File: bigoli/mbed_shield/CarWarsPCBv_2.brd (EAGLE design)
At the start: 68.6 x 55.9 mm, 22 parts, among them J1 MAGJACK, Q1 220mA/50V/3.5Ω, Q2 220mA/50V/3.5Ω

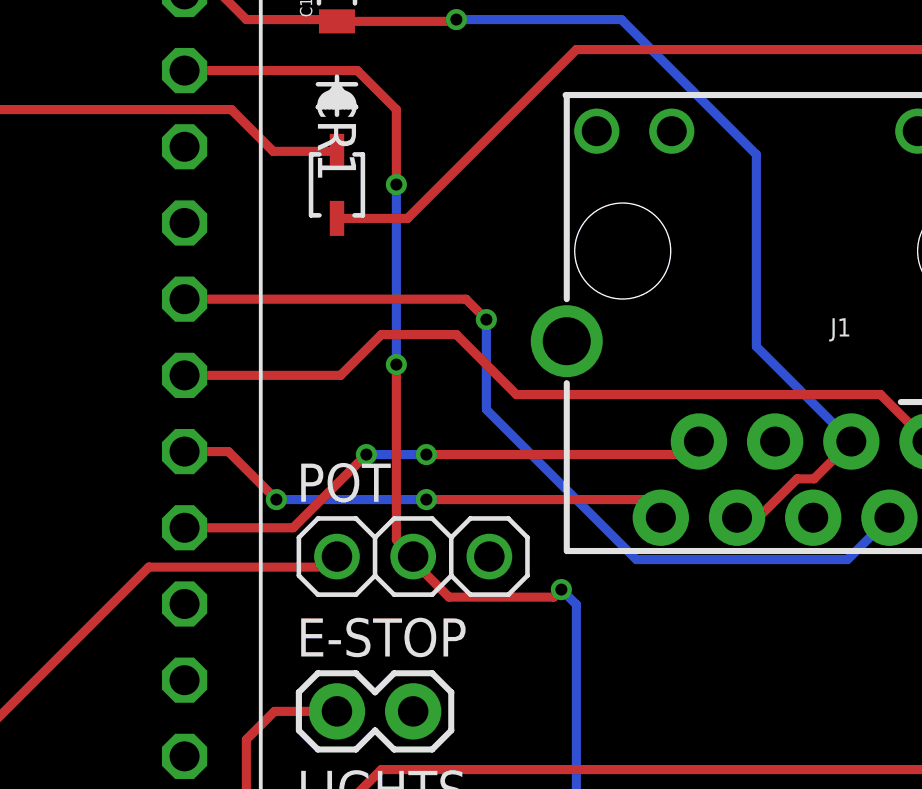
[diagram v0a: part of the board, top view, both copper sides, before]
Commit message: Fixed Routing so Pot runs at 3v3.  Added Resistor and Capacitor Values.
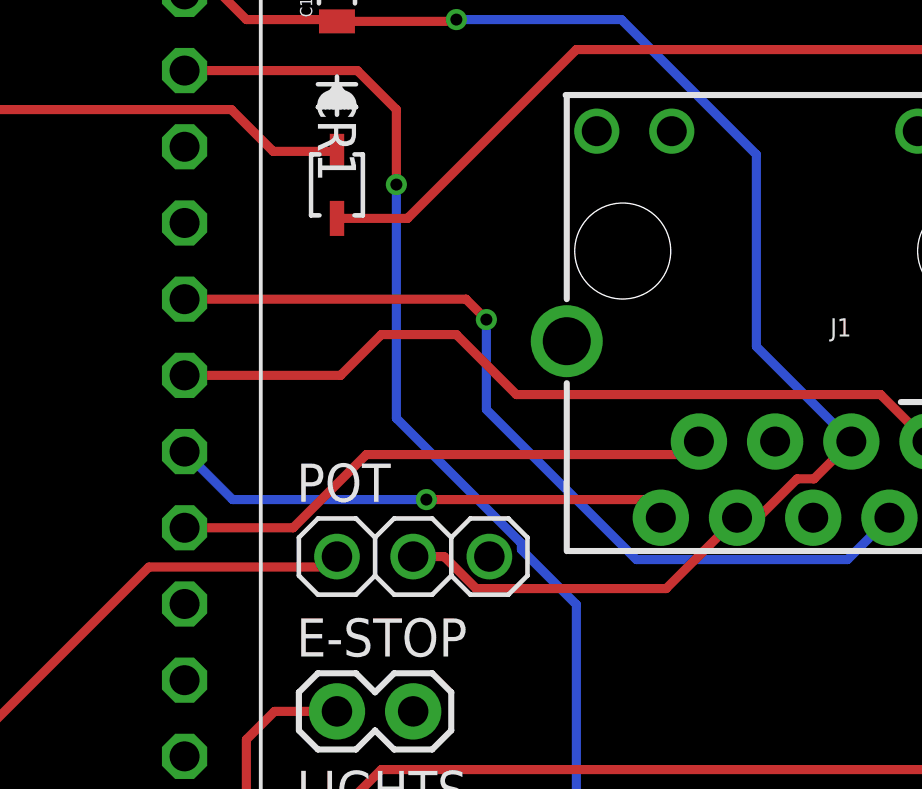
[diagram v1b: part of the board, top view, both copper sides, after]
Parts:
- C2: value (none) -> 1000PF
- R5, R6: value 62 -> 1K
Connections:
- net +3V3: now also POT.2
- net +5V: no longer POT.2
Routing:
- net +3V3: track 37.1 -> 49.3 mm
- net +5V: track 77.5 -> 75.0 mm, vias 4 -> 2
- net ETH_TD+: track 18.3 -> 18.9 mm, vias 2 -> 0
- net ETH_TD-: vias 2 -> 1
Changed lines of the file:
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@@
 <?xml version="1.0" encoding="utf-8"?>
 <!DOCTYPE eagle SYSTEM "eagle.dtd">
-<eagle version="8.2.1">
+<eagle version="8.3.2">
 <drawing>
 <settings>
 <setting alwaysvectorfont="no"/>
+<setting keepoldvectorfont="yes"/>
 <setting verticaltext="up"/>
 </settings>
@@
 <layers>
 <layer number="1" name="Top" color="4" fill="1" visible="yes" active="yes"/>
-<layer number="2" name="Route2" color="1" fill="3" visible="no" active="yes"/>
+<layer number="2" name="Route2" color="1" fill="3" visible="yes" active="yes"/>
 <layer number="3" name="Route3" color="4" fill="3" visible="no" active="yes"/>
 <layer number="4" name="Route4" color="1" fill="4" visible="no" active="yes"/>
@@
 <element name="R3" library="rcl" library_urn="urn:adsk.eagle:library:334" package="R0603" value="10K" x="49.76" y="21.82" rot="R270"/>
 <element name="R4" library="rcl" library_urn="urn:adsk.eagle:library:334" package="R0603" value="10K" x="49.76" y="10.35" rot="R90"/>
-<element name="R5" library="rcl" library_urn="urn:adsk.eagle:library:334" package="R0603" value="62" x="53.57" y="10.35" rot="R270"/>
-<element name="R6" library="rcl" library_urn="urn:adsk.eagle:library:334" package="R0603" value="62" x="53.57" y="21.82" rot="R90"/>
+<element name="R5" library="rcl" library_urn="urn:adsk.eagle:library:334" package="R0603" value="1K" x="53.57" y="10.35" rot="R270"/>
+<element name="R6" library="rcl" library_urn="urn:adsk.eagle:library:334" package="R0603" value="1K" x="53.57" y="21.82" rot="R90"/>
 <element name="STEER" library="Roboracing" package="1X03" value="" x="35.56" y="9.2"/>
-<element name="C2" library="rcl" library_urn="urn:adsk.eagle:library:334" package="C0805" value="" x="60.96" y="38.1"/>
+<element name="C2" library="rcl" library_urn="urn:adsk.eagle:library:334" package="C0805" value="1000PF" x="60.96" y="38.1"/>
 </elements>
 <signals>
@@
 <wire x1="43.21" y1="36.5" x2="36" y2="36.5" width="0.3048" layer="1"/>
 <via x="36" y="36.5" extent="1-16" drill="0.4"/>
-<wire x1="36" y1="36.5" x2="31" y2="36.5" width="0.3048" layer="16"/>
-<via x="31" y="36.5" extent="1-16" drill="0.4"/>
-<wire x1="31" y1="36.5" x2="29.4" y2="38.1" width="0.3048" layer="1"/>
-<wire x1="29.4" y1="38.1" x2="27.94" y2="38.1" width="0.3048" layer="1"/>
+<wire x1="36" y1="36.5" x2="29.54" y2="36.5" width="0.3048" layer="16"/>
+<wire x1="29.54" y1="36.5" x2="27.94" y2="38.1" width="0.3048" layer="16"/>
 </signal>
 <signal name="ETH_TD+">
 <contactref element="MBED" pad="33"/>
 <contactref element="J1" pad="7"/>
-<via x="36" y="38" extent="1-16" drill="0.4"/>
-<wire x1="36" y1="38" x2="34" y2="38" width="0.3048" layer="16"/>
-<via x="34" y="38" extent="1-16" drill="0.4"/>
-<wire x1="36" y1="38" x2="44.65" y2="38" width="0.3048" layer="1"/>
-<wire x1="44.65" y1="38" x2="45.085" y2="38.435" width="0.3048" layer="1"/>
+<wire x1="45.075" y1="38.425" x2="45.085" y2="38.435" width="0.3048" layer="1"/>
+<wire x1="45.075" y1="38.425" x2="44.65" y2="38" width="0.3048" layer="1"/>
 <wire x1="27.94" y1="35.56" x2="31.56" y2="35.56" width="0.3048" layer="1"/>
 <wire x1="31.56" y1="35.56" x2="34" y2="38" width="0.3048" layer="1"/>
+<wire x1="34" y1="38" x2="44.65" y2="38" width="0.3048" layer="1"/>
+<wire x1="44.65" y1="38" x2="45.075" y2="38.425" width="0.3048" layer="1"/>
 </signal>
 <signal name="GND">
@@
 <wire x1="46.355" y1="35.895" x2="47.063025" y2="35.895" width="0.3048" layer="1"/>
 <wire x1="47.063025" y1="35.895" x2="48.358425" y2="37.1904" width="0.3048" layer="1"/>
+<contactref element="POT" pad="2"/>
+<wire x1="35.56" y1="34.6" x2="36.5913125" y2="34.6" width="0.3048" layer="1"/>
+<wire x1="36.5913125" y1="34.6" x2="37.6581125" y2="33.5332" width="0.3048" layer="1"/>
+<wire x1="37.6581125" y1="33.5332" x2="43.9932" y2="33.5332" width="0.3048" layer="1"/>
+<wire x1="43.9932" y1="33.5332" x2="46.355" y2="35.895" width="0.3048" layer="1"/>
 </signal>
 <signal name="DRIVE_PWM_3V3">
@@
 <contactref element="MBED" pad="39"/>
 <contactref element="ENCODER" pad="4"/>
-<contactref element="POT" pad="2"/>
 <contactref element="R5" pad="2"/>
 <contactref element="R6" pad="2"/>
@@
 <wire x1="35" y1="49.5" x2="35" y2="47" width="0.3048" layer="1"/>
 <via x="35" y="47" extent="1-16" drill="0.4"/>
-<wire x1="35" y1="47" x2="35" y2="41" width="0.3048" layer="16"/>
-<via x="35" y="41" extent="1-16" drill="0.4"/>
-<wire x1="35" y1="35.16" x2="35" y2="41" width="0.3048" layer="1"/>
-<wire x1="35" y1="35.16" x2="35.56" y2="34.6" width="0.3048" layer="1"/>
-<via x="40.5" y="33.5" extent="1-16" drill="0.4"/>
-<wire x1="40.5" y1="33.5" x2="41" y2="33" width="0.3048" layer="16"/>
+<wire x1="35" y1="47" x2="35" y2="39.2086875" width="0.3048" layer="16"/>
 <wire x1="41" y1="33" x2="41" y2="26.5" width="0.3048" layer="16"/>
 <via x="41" y="26.5" extent="1-16" drill="0.4"/>
@@
 <wire x1="54" y1="9.5" x2="53.57" y2="9.5" width="0.3048" layer="1"/>
 <wire x1="54.5" y1="10" x2="54" y2="9.5" width="0.3048" layer="1"/>
-<wire x1="35.56" y1="34.6" x2="35.56" y2="34.44" width="0.3048" layer="1"/>
-<wire x1="35.56" y1="34.44" x2="36.75" y2="33.25" width="0.3048" layer="1"/>
-<wire x1="36.75" y1="33.25" x2="40.25" y2="33.25" width="0.3048" layer="1"/>
-<wire x1="40.25" y1="33.25" x2="40.5" y2="33.5" width="0.3048" layer="1"/>
+<wire x1="39.1668" y1="35.0418875" x2="39.1668" y2="34.8332" width="0.3048" layer="16"/>
+<wire x1="35" y1="39.2086875" x2="39.1668" y2="35.0418875" width="0.3048" layer="16"/>
+<wire x1="39.1668" y1="34.8332" x2="41" y2="33" width="0.3048" layer="16"/>
 </signal>
 <signal name="STEER_POT">
@@
 <compatibility>
 <note version="8.2" severity="warning">
-Since Version 8.2, Eagle supports online libraries. The ids
+Since Version 8.2, EAGLE supports online libraries. The ids
 of those online libraries will not be understood (or retained)
 with this version.

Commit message: Improve routing efficiency
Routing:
- net VCC: track 92.6 -> 91.2 mm
- net ETH_RD+: track 26.8 -> 25.7 mm
- net +5V: track 75.0 -> 76.0 mm, vias 2 -> 1
- net DRIVE_PWM_3V3: track 29.9 -> 30.6 mm
- net ETH_TD+: track 18.9 -> 18.3 mm
- net V_SENSE: vias 2 -> 0
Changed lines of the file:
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@@
 <?xml version="1.0" encoding="utf-8"?>
 <!DOCTYPE eagle SYSTEM "eagle.dtd">
-<eagle version="8.3.2">
+<eagle version="8.3.1">
 <drawing>
 <settings>
@@
 <layer number="1" name="Top" color="4" fill="1" visible="yes" active="yes"/>
 <layer number="2" name="Route2" color="1" fill="3" visible="yes" active="yes"/>
-<layer number="3" name="Route3" color="4" fill="3" visible="no" active="yes"/>
+<layer number="3" name="Route3" color="4" fill="3" visible="yes" active="yes"/>
 <layer number="4" name="Route4" color="1" fill="4" visible="no" active="yes"/>
 <layer number="5" name="Route5" color="4" fill="4" visible="no" active="yes"/>
@@
 <contactref element="MBED" pad="36"/>
 <contactref element="J1" pad="2"/>
-<wire x1="27.94" y1="43.18" x2="37.32" y2="43.18" width="0.3048" layer="1"/>
-<wire x1="37.32" y1="43.18" x2="38" y2="42.5" width="0.3048" layer="1"/>
 <via x="38" y="42.5" extent="1-16" drill="0.4"/>
 <wire x1="38" y1="42.5" x2="38" y2="39.5" width="0.3048" layer="16"/>
@@
 <wire x1="43" y1="34.5" x2="50.04" y2="34.5" width="0.3048" layer="16"/>
 <wire x1="50.04" y1="34.5" x2="51.435" y2="35.895" width="0.3048" layer="16"/>
+<wire x1="38" y1="42.5" x2="28.62" y2="42.5" width="0.3048" layer="1"/>
+<wire x1="28.62" y1="42.5" x2="27.94" y2="43.18" width="0.3048" layer="1"/>
 </signal>
 <signal name="ETH_RD+">
 <contactref element="MBED" pad="35"/>
 <contactref element="J1" pad="1"/>
-<wire x1="27.94" y1="40.64" x2="33.14" y2="40.64" width="0.3048" layer="1"/>
-<wire x1="33.14" y1="40.64" x2="34.5" y2="42" width="0.3048" layer="1"/>
-<wire x1="34.5" y1="42" x2="37" y2="42" width="0.3048" layer="1"/>
-<wire x1="37" y1="42" x2="39" y2="40" width="0.3048" layer="1"/>
-<wire x1="39" y1="40" x2="51.14" y2="40" width="0.3048" layer="1"/>
-<wire x1="51.14" y1="40" x2="52.705" y2="38.435" width="0.3048" layer="1"/>
+<wire x1="52.705" y1="38.435" x2="51.14" y2="40" width="0.3048" layer="1"/>
+<wire x1="28.58" y1="40" x2="27.94" y2="40.64" width="0.3048" layer="1"/>
+<wire x1="51.14" y1="40" x2="28.58" y2="40" width="0.3048" layer="1"/>
 </signal>
 <signal name="ETH_TD-">
@@
 <contactref element="MBED" pad="33"/>
 <contactref element="J1" pad="7"/>
-<wire x1="45.075" y1="38.425" x2="45.085" y2="38.435" width="0.3048" layer="1"/>
-<wire x1="45.075" y1="38.425" x2="44.65" y2="38" width="0.3048" layer="1"/>
-<wire x1="27.94" y1="35.56" x2="31.56" y2="35.56" width="0.3048" layer="1"/>
-<wire x1="31.56" y1="35.56" x2="34" y2="38" width="0.3048" layer="1"/>
-<wire x1="34" y1="38" x2="44.65" y2="38" width="0.3048" layer="1"/>
-<wire x1="44.65" y1="38" x2="45.075" y2="38.425" width="0.3048" layer="1"/>
+<wire x1="27.94" y1="35.56" x2="29.06" y2="35.56" width="0.3048" layer="1"/>
+<wire x1="29.06" y1="35.56" x2="31.5" y2="38" width="0.3048" layer="1"/>
+<wire x1="31.5" y1="38" x2="44.65" y2="38" width="0.3048" layer="1"/>
+<wire x1="44.65" y1="38" x2="45.085" y2="38.435" width="0.3048" layer="1"/>
 </signal>
 <signal name="GND">
@@
 <contactref element="Q2" pad="1"/>
 <contactref element="R4" pad="2"/>
-<wire x1="27.94" y1="5.08" x2="41.08" y2="5.08" width="0.3048" layer="1"/>
-<wire x1="45.5" y1="11.48011875" x2="45.5" y2="11.20875" width="0.3048" layer="1"/>
-<wire x1="45.5" y1="11.48011875" x2="45.5" y2="14" width="0.3048" layer="1"/>
+<wire x1="45.5" y1="11" x2="45.5" y2="14" width="0.3048" layer="1"/>
 <wire x1="46.11" y1="15.11" x2="46.45" y2="15.11" width="0.3048" layer="1"/>
 <wire x1="45.5" y1="14" x2="46.11" y2="15.11" width="0.3048" layer="1"/>
 <wire x1="49.76" y1="11.2" x2="49.75125" y2="11.20875" width="0.3048" layer="1"/>
-<wire x1="41.08" y1="5.08" x2="45.5" y2="9.5" width="0.3048" layer="1"/>
-<wire x1="45.5" y1="9.5" x2="45.5" y2="11" width="0.3048" layer="1"/>
-<wire x1="45.5" y1="11" x2="45.5" y2="11.20875" width="0.3048" layer="1"/>
+<wire x1="45.5" y1="9.62058125" x2="45.5" y2="9.5" width="0.3048" layer="1"/>
+<wire x1="45.5" y1="9.62058125" x2="45.5" y2="11" width="0.3048" layer="1"/>
 <wire x1="45.5" y1="11" x2="49.56" y2="11" width="0.3048" layer="1"/>
 <wire x1="49.56" y1="11" x2="49.76" y2="11.2" width="0.3048" layer="1"/>
+<wire x1="27.94" y1="5.08" x2="42.08" y2="5.08" width="0.3048" layer="1"/>
+<wire x1="42.08" y1="5.08" x2="45.5" y2="8.5" width="0.3048" layer="1"/>
+<wire x1="45.5" y1="8.5" x2="45.5" y2="9.62058125" width="0.3048" layer="1"/>
 </signal>
 <signal name="STEER_PWM">
@@
 <contactref element="R5" pad="2"/>
 <contactref element="R6" pad="2"/>
-<wire x1="27.94" y1="50.8" x2="33.7" y2="50.8" width="0.3048" layer="1"/>
-<wire x1="33.7" y1="50.8" x2="35" y2="49.5" width="0.3048" layer="1"/>
-<wire x1="35" y1="49.5" x2="35" y2="47" width="0.3048" layer="1"/>
-<via x="35" y="47" extent="1-16" drill="0.4"/>
-<wire x1="35" y1="47" x2="35" y2="39.2086875" width="0.3048" layer="16"/>
-<wire x1="41" y1="33" x2="41" y2="26.5" width="0.3048" layer="16"/>
 <via x="41" y="26.5" extent="1-16" drill="0.4"/>
 <wire x1="40.64" y1="26.14" x2="41" y2="26.5" width="0.3048" layer="1"/>
@@
 <wire x1="54" y1="9.5" x2="53.57" y2="9.5" width="0.3048" layer="1"/>
 <wire x1="54.5" y1="10" x2="54" y2="9.5" width="0.3048" layer="1"/>
-<wire x1="39.1668" y1="35.0418875" x2="39.1668" y2="34.8332" width="0.3048" layer="16"/>
-<wire x1="35" y1="39.2086875" x2="39.1668" y2="35.0418875" width="0.3048" layer="16"/>
-<wire x1="39.1668" y1="34.8332" x2="41" y2="33" width="0.3048" layer="16"/>
+<wire x1="41" y1="34.5" x2="36.5" y2="39" width="0.3048" layer="16"/>
+<wire x1="41" y1="26.5" x2="41" y2="34.5" width="0.3048" layer="16"/>
+<wire x1="36.5" y1="39" x2="36.5" y2="49.5" width="0.3048" layer="16"/>
+<wire x1="36.5" y1="49.5" x2="35" y2="51" width="0.3048" layer="16"/>
+<wire x1="35" y1="51" x2="28.14" y2="51" width="0.3048" layer="16"/>
+<wire x1="28.14" y1="51" x2="27.94" y2="50.8" width="0.3048" layer="16"/>
 </signal>
 <signal name="STEER_POT">
@@
 <contactref element="CR1" pad="2"/>
 <contactref element="C2" pad="1"/>
-<wire x1="60.01" y1="40.01" x2="60.01" y2="38.1" width="0.3048" layer="1"/>
+<wire x1="60.01" y1="38.191771875" x2="60.01" y2="40.01" width="0.3048" layer="1"/>
+<wire x1="60.01" y1="38.191771875" x2="60.01" y2="38.1" width="0.3048" layer="1"/>
 <wire x1="62.18" y1="42.18" x2="64.77" y2="42.18" width="0.3048" layer="1"/>
 <wire x1="60.01" y1="40.01" x2="62.18" y2="42.18" width="0.3048" layer="1"/>
-<wire x1="60.01" y1="38.1" x2="60.01" y2="30.01" width="0.3048" layer="1"/>
-<wire x1="57.5" y1="27.5" x2="34.5" y2="27.5" width="0.3048" layer="1"/>
-<wire x1="33.02" y1="26.02" x2="33.02" y2="24.36" width="0.3048" layer="1"/>
-<wire x1="60.01" y1="30.01" x2="57.5" y2="27.5" width="0.3048" layer="1"/>
-<wire x1="34.5" y1="27.5" x2="33.02" y2="26.02" width="0.3048" layer="1"/>
 <wire x1="64.77" y1="42.18" x2="65.18" y2="42.18" width="0.3048" layer="1"/>
 <wire x1="65.18" y1="42.18" x2="67.5" y2="44.5" width="0.3048" layer="1"/>
@@
 <wire x1="35.3724" y1="45.8724" x2="33.02" y2="45.8724" width="0.3048" layer="1"/>
 <wire x1="41" y1="51.5" x2="35.3724" y2="45.8724" width="0.3048" layer="1"/>
-<wire x1="60.01" y1="30.01" x2="60.01" y2="29.99" width="0.3048" layer="1"/>
+<wire x1="33.02" y1="24.36" x2="33.02" y2="26.02" width="0.3048" layer="1"/>
+<wire x1="33.02" y1="26.02" x2="34.5" y2="27.5" width="0.3048" layer="1"/>
+<wire x1="34.5" y1="27.5" x2="55" y2="27.5" width="0.3048" layer="1"/>
+<wire x1="55" y1="27.5" x2="60" y2="32.5" width="0.3048" layer="1"/>
+<wire x1="60" y1="32.5" x2="60" y2="38.181771875" width="0.3048" layer="1"/>
+<wire x1="60" y1="38.181771875" x2="60.01" y2="38.191771875" width="0.3048" layer="1"/>
 </signal>
 <signal name="I_SENSE">
@@
 <contactref element="IV_SENSOR" pad="2"/>
 <contactref element="MBED" pad="16"/>
-<wire x1="35.56" y1="19.52" x2="33.04" y2="17" width="0.3048" layer="1"/>
-<wire x1="33.04" y1="17" x2="32" y2="17" width="0.3048" layer="1"/>
-<via x="32" y="17" extent="1-16" drill="0.4"/>
 <wire x1="32" y1="17" x2="31.5" y2="16.5" width="0.3048" layer="16"/>
-<wire x1="31.5" y1="16.5" x2="25" y2="16.5" width="0.3048" layer="16"/>
-<via x="25" y="16.5" extent="1-16" drill="0.4"/>
-<wire x1="25" y1="16.5" x2="23.74" y2="15.24" width="0.3048" layer="1"/>
-<wire x1="23.74" y1="15.24" x2="5.08" y2="15.24" width="0.3048" layer="1"/>
+<wire x1="32" y1="17" x2="33.04" y2="17" width="0.3048" layer="16"/>
+<wire x1="33.04" y1="17" x2="35.56" y2="19.52" width="0.3048" layer="16"/>
+<wire x1="6.34" y1="16.5" x2="5.08" y2="15.24" width="0.3048" layer="16"/>
+<wire x1="31.5" y1="16.5" x2="6.34" y2="16.5" width="0.3048" layer="16"/>
 </signal>
 <signal name="N$1">
